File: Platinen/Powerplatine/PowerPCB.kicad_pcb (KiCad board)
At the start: 2 copper layers, 300 x 210 mm, 35 parts, among them J1 Eingangsbuchse, J2 Conn_01x03_Pin, J3 Conn_01x03_Pin, J4 Conn_01x03_Socket, J5 Conn_01x03_Socket, U1 Generic DCDC, X1 Conn_01x03_Pin, X10 Conn_01x03_Pin, X11 Conn_01x03_Pin, X12 Conn_01x03_Pin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

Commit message: Changed pins to sockets, added image
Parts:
- X1, X10, X11, X12, X13, X14, X15, X16, X17, X18, X19, X2, X3, X4, X5, X6, X7, X8, X9: footprint Connector_PinHeader_2.54mm:PinHeader_1x03_P2.54mm_Vertical -> Connector_PinSocket_2.54mm:PinSocket_1x03_P2.54mm_Vertical
- moved C2 229.7 mm to (333.1, 37.0)
- moved X16 229.7 mm to (324.7, 33.3)
- moved X17 229.7 mm to (341.3, 33.3)
- moved X18 229.7 mm to (358.0, 33.3)
- moved H3 229.7 mm to (302.2, 36.3)
- moved H5 229.7 mm to (391.7, 36.5)
- moved J5 229.7 mm to (296.8, 37.0)
- moved X14 229.7 mm to (291.3, 33.3)
- moved X15 229.7 mm to (308.0, 33.3)
- moved X19 229.7 mm to (374.7, 33.3)
- moved J3 116.9 mm to (277.6, 37.1)
- moved H4 116.9 mm to (202.0, 36.6)
- moved J4 116.9 mm to (183.9, 37.0)
- moved X10 116.9 mm to (224.9, 33.3)
- moved X11 116.9 mm to (241.4, 33.4)
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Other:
- board size 300 x 210 mm -> 339 x 29.9 mm

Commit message: added letter matrix pdf v1
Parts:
- moved H2 24.5 mm to (122.0, 37.0)
- moved H1 1.27 mm to (62.0, 55.0)
- moved H3 0.73 mm to (302.0, 37.0)
- moved H5 0.54 mm to (392.0, 37.0)
- moved H4 0.40 mm to (202.0, 37.0)
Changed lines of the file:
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@@
 	(footprint "MountingHole:MountingHole_3.2mm_M3_DIN965"
 		(layer "F.Cu")
-		(at 391.7 36.55)
+		(at 392 37)
 		(descr "Mounting Hole 3.2mm, no annular, M3, DIN965")
 		(tags "mounting hole 3.2mm no annular m3 din965")
@@
 	(footprint "MountingHole:MountingHole_3.2mm_M3_DIN965"
 		(layer "F.Cu")
-		(at 63.25 54.75)
+		(at 62 55)
 		(descr "Mounting Hole 3.2mm, no annular, M3, DIN965")
 		(tags "mounting hole 3.2mm no annular m3 din965")
@@
 	(footprint "MountingHole:MountingHole_3.2mm_M3_DIN965"
 		(layer "F.Cu")
-		(at 302.2 36.3)
+		(at 302 37)
 		(descr "Mounting Hole 3.2mm, no annular, M3, DIN965")
 		(tags "mounting hole 3.2mm no annular m3 din965")
@@
 	(footprint "MountingHole:MountingHole_3.2mm_M3_DIN965"
 		(layer "F.Cu")
-		(at 202 36.6)
+		(at 202 37)
 		(descr "Mounting Hole 3.2mm, no annular, M3, DIN965")
 		(tags "mounting hole 3.2mm no annular m3 din965")
@@
 	(footprint "MountingHole:MountingHole_3.2mm_M3_DIN965"
 		(layer "F.Cu")
-		(at 144.25 47.25)
+		(at 122 37)
 		(descr "Mounting Hole 3.2mm, no annular, M3, DIN965")
 		(tags "mounting hole 3.2mm no annular m3 din965")
@@
 		(layer "Margin")
 	)
+	(dimension
+		(type orthogonal)
+		(layer "Edge.Cuts")
+		(pts
+			(xy 170.8 60.4) (xy 170.8 30.6)
+		)
+		(height 5)
+		(orientation 1)
+		(format
+			(prefix "")
+			(suffix "")
+			(units 3)
+			(units_format 0)
+			(precision 4)
+			(suppress_zeroes yes)
+		)
+		(style
+			(thickness 0.05)
+			(arrow_length 1.27)
+			(text_position_mode 0)
+			(arrow_direction outward)
+			(extension_height 0.58642)
+			(extension_offset 0.5)
+			(keep_text_aligned yes)
+		)
+		(gr_text "29.8"
+			(at 174.65 45.5 90)
+			(layer "Edge.Cuts")
+			(effects
+				(font
+					(size 1 1)
+					(thickness 0.15)
+				)
+			)
+		)
+	)
 	(segment

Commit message: Adjusted letter matrix and added stencil verśion
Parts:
- added FID1: Fiducial, Fiducial:Fiducial_1.5mm_Mask3mm, F.Cu at (60.3, 33.2)
- added FID2: Fiducial, Fiducial:Fiducial_1.5mm_Mask3mm, F.Cu at (60.5, 80.4)
- added FID3: Fiducial, Fiducial:Fiducial_1.5mm_Mask3mm, F.Cu at (161.8, 80.6)
- X1, X10, X11, X12, X13, X14, X15, X16, X17, X18, X19, X2, X3, X4, X5, X6, X7, X8, X9: footprint Connector_PinSocket_2.54mm:PinSocket_1x03_P2.54mm_Vertical -> Connector_PinHeader_2.54mm:PinHeader_1x03_P2.54mm_Vertical
- moved C2 229.7 mm to (107.2, 78.2)
- moved X16 229.7 mm to (98.7, 74.5)
- moved X17 229.7 mm to (115.4, 74.5)
- moved X18 229.7 mm to (132.0, 74.5)
- moved H3 229.7 mm to (76.0, 78.2)
- moved H5 229.7 mm to (166.1, 78.2)
- moved J5 229.7 mm to (70.9, 78.2)
- moved X14 229.7 mm to (65.4, 74.5)
- moved X15 229.7 mm to (82.1, 74.5)
- moved X19 229.7 mm to (148.7, 74.5)
- moved J3 116.9 mm to (164.6, 66.9)
- moved H4 116.9 mm to (89.0, 66.9)
- moved J4 116.9 mm to (70.9, 66.9)
- moved X10 116.9 mm to (111.9, 63.2)
- moved X11 116.9 mm to (128.4, 63.2)
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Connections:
- J3 pad 2: Net-(J3-Pin_2) -> unconnected-(J3-Pin_2-Pad2)
- J5 pad 2: Net-(J5-Pin_2) -> unconnected-(J5-Pin_2-Pad2)
- X1 pad 2: Net-(X1-Pin_2) -> unconnected-(X1-Pin_2-Pad2)
- X11 pad 2: Net-(X11-Pin_2) -> Net-(X10-Pin_2)
- X12 pad 2: Net-(X11-Pin_2) -> Net-(X12-Pin_2)
- X13 pad 2: Net-(J3-Pin_2) -> Net-(X12-Pin_2)
- X14 pad 2: Net-(J5-Pin_2) -> Net-(X14-Pin_2)
- X15 pad 2: Net-(X15-Pin_2) -> Net-(X14-Pin_2)
- X16 pad 2: Net-(X15-Pin_2) -> Net-(X16-Pin_2)
- X17 pad 2: Net-(X17-Pin_2) -> Net-(X16-Pin_2)
- X18 pad 2: Net-(X17-Pin_2) -> Net-(X18-Pin_2)
- X19 pad 2: unconnected-(X19-Pin_2-Pad2) -> Net-(X18-Pin_2)
- X2 pad 2: Net-(X1-Pin_2) -> Net-(X2-Pin_2)
- X3 pad 2: Net-(X3-Pin_2) -> Net-(X2-Pin_2)
- X4 pad 2: Net-(X3-Pin_2) -> Net-(X4-Pin_2)
- X5 pad 2: Net-(J2-Pin_2) -> Net-(X4-Pin_2)
- X8 pad 2: Net-(J4-Pin_2) -> Net-(X8-Pin_2)
- X9 pad 2: Net-(X10-Pin_2) -> Net-(X8-Pin_2)
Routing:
- net Net-(X17-Pin_2): track 18.7 -> 0.00 mm
- net Net-(X3-Pin_2): track 18.7 -> 0.00 mm
- net Net-(X1-Pin_2): track 18.7 -> 0.00 mm
- net Net-(X15-Pin_2): track 18.7 -> 0.00 mm
- net Net-(X11-Pin_2): track 18.7 -> 0.00 mm
- net Net-(X14-Pin_2): track 0.00 -> 18.6 mm
- net Net-(X12-Pin_2): track 0.00 -> 18.6 mm
- net Net-(X16-Pin_2): track 0.00 -> 18.2 mm
- net Net-(X2-Pin_2): track 0.00 -> 18.2 mm
- net Net-(X4-Pin_2): track 0.00 -> 18.2 mm
- net Net-(X18-Pin_2): track 0.00 -> 18.2 mm
- net Net-(X8-Pin_2): track 0.00 -> 18.2 mm
- net Net-(X10-Pin_2): track 0.00 -> 18.0 mm
- net Net-(J4-Pin_2): track 18.7 -> 7.38 mm
- net Net-(J2-Pin_2): track 18.7 -> 8.66 mm
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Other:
- board size 339 x 29.9 mm -> 113 x 52.4 mm

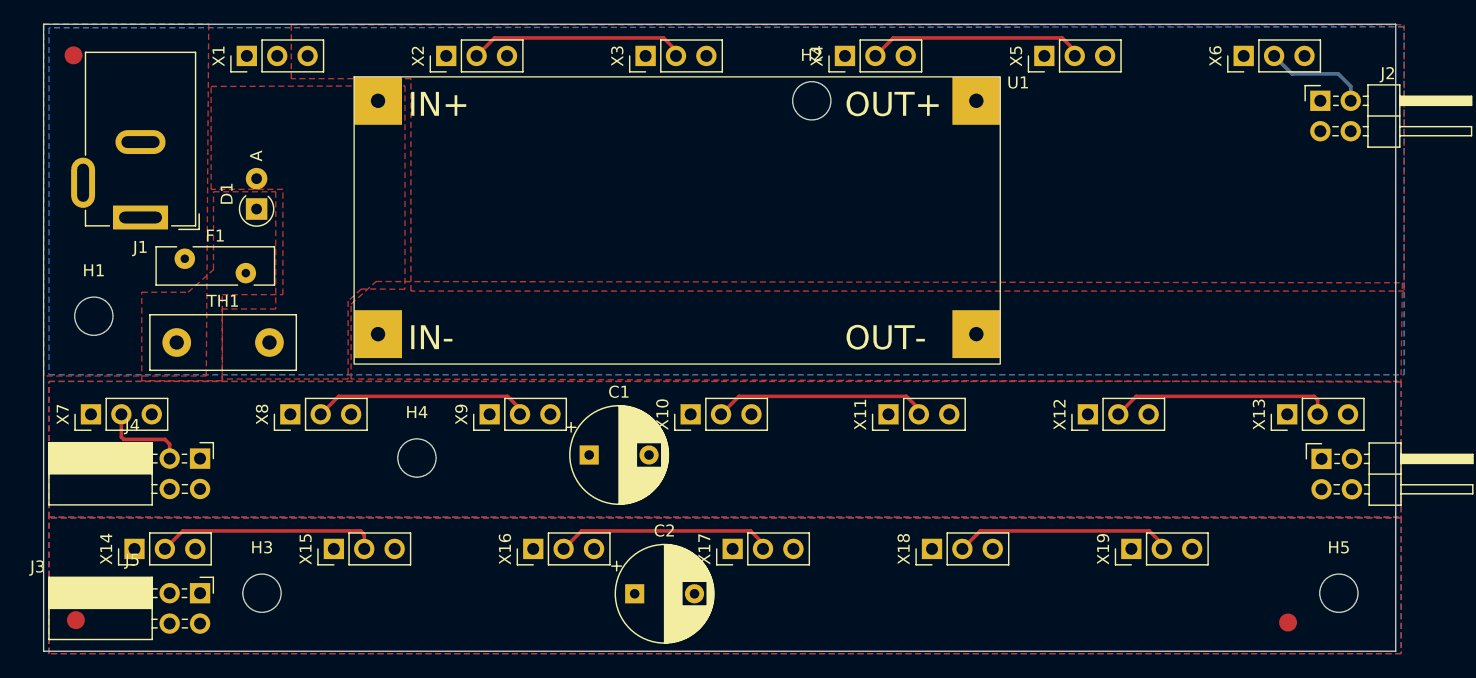
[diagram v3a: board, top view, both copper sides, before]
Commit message: added trotec template
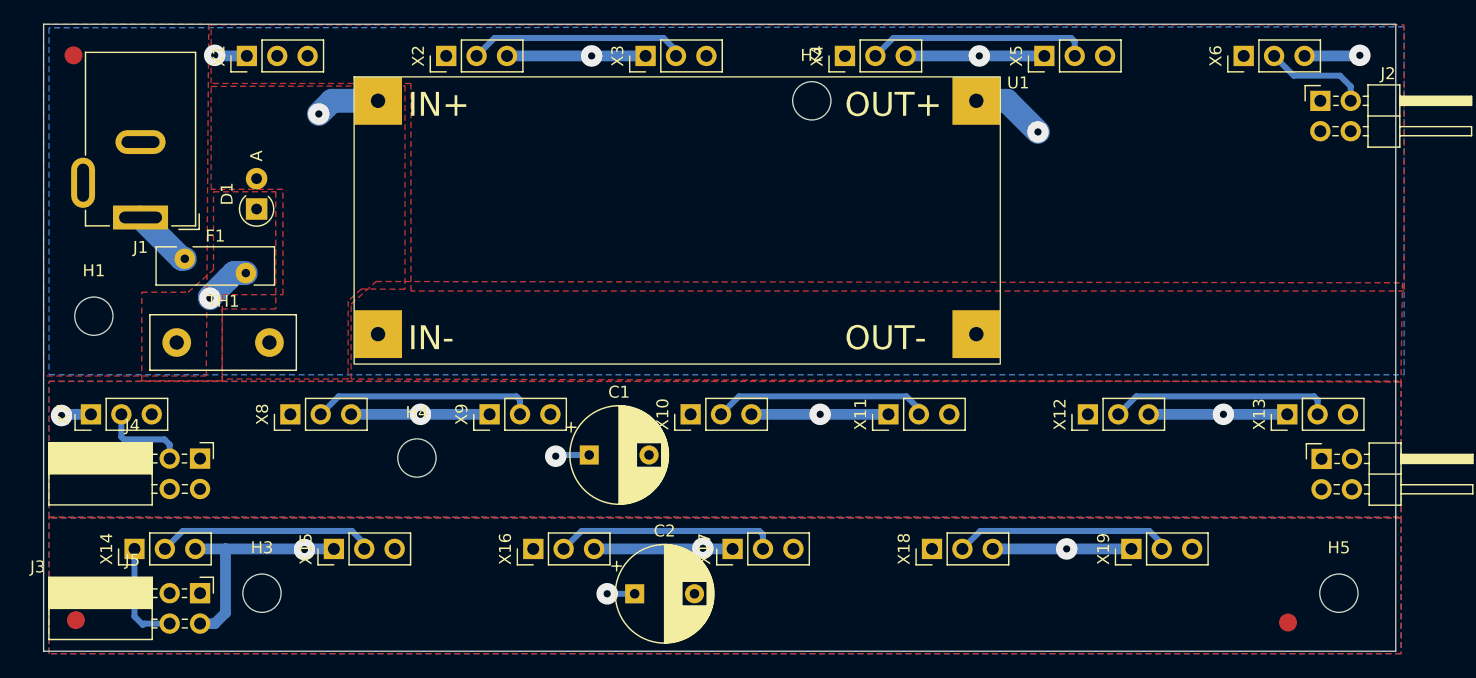
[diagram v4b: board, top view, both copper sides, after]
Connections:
- X1 pad 1: GND -> +5V
- X1 pad 3: +5V -> GND
- X11 pad 1: GND2 -> +5V2
- X11 pad 3: +5V2 -> GND2
- X13 pad 1: GND2 -> +5V2
- X13 pad 3: +5V2 -> GND2
- X15 pad 1: GND3 -> +5V3
- X15 pad 3: +5V3 -> GND3
- X17 pad 1: GND3 -> +5V3
- X17 pad 3: +5V3 -> GND3
- X19 pad 1: GND3 -> +5V3
- X19 pad 3: +5V3 -> GND3
- X3 pad 1: GND -> +5V
- X3 pad 3: +5V -> GND
- X5 pad 1: GND -> +5V
- X5 pad 3: +5V -> GND
- X7 pad 1: GND2 -> +5V2
- X7 pad 3: +5V2 -> GND2
- X9 pad 1: GND2 -> +5V2
- X9 pad 3: +5V2 -> GND2
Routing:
- net +5V3: track 0.00 -> 45.0 mm, vias 0 -> 4
- net +5V2: track 0.00 -> 39.9 mm, vias 0 -> 5
- net +5V: track 0.00 -> 36.7 mm, vias 0 -> 5
- net GND3: track 0.00 -> 8.92 mm
- net Net-(U1-IN): track 0.00 -> 5.41 mm, vias 0 -> 1
- net Net-(F1-Pad1): track 0.00 -> 5.13 mm
- net Net-(D1-K): track 0.00 -> 3.93 mm, vias 0 -> 1
